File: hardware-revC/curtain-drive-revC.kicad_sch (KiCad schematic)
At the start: 45 parts, among them J1 12V IN, J3 MOTOR, J4 ENCODER I2C, J5 UART, SW1 USER, SW2 BOOT, SW3 RESET, U1 ESP32-WROOM-32, U2 L298, U3 LM2575T-ADJ, U4 LM7805

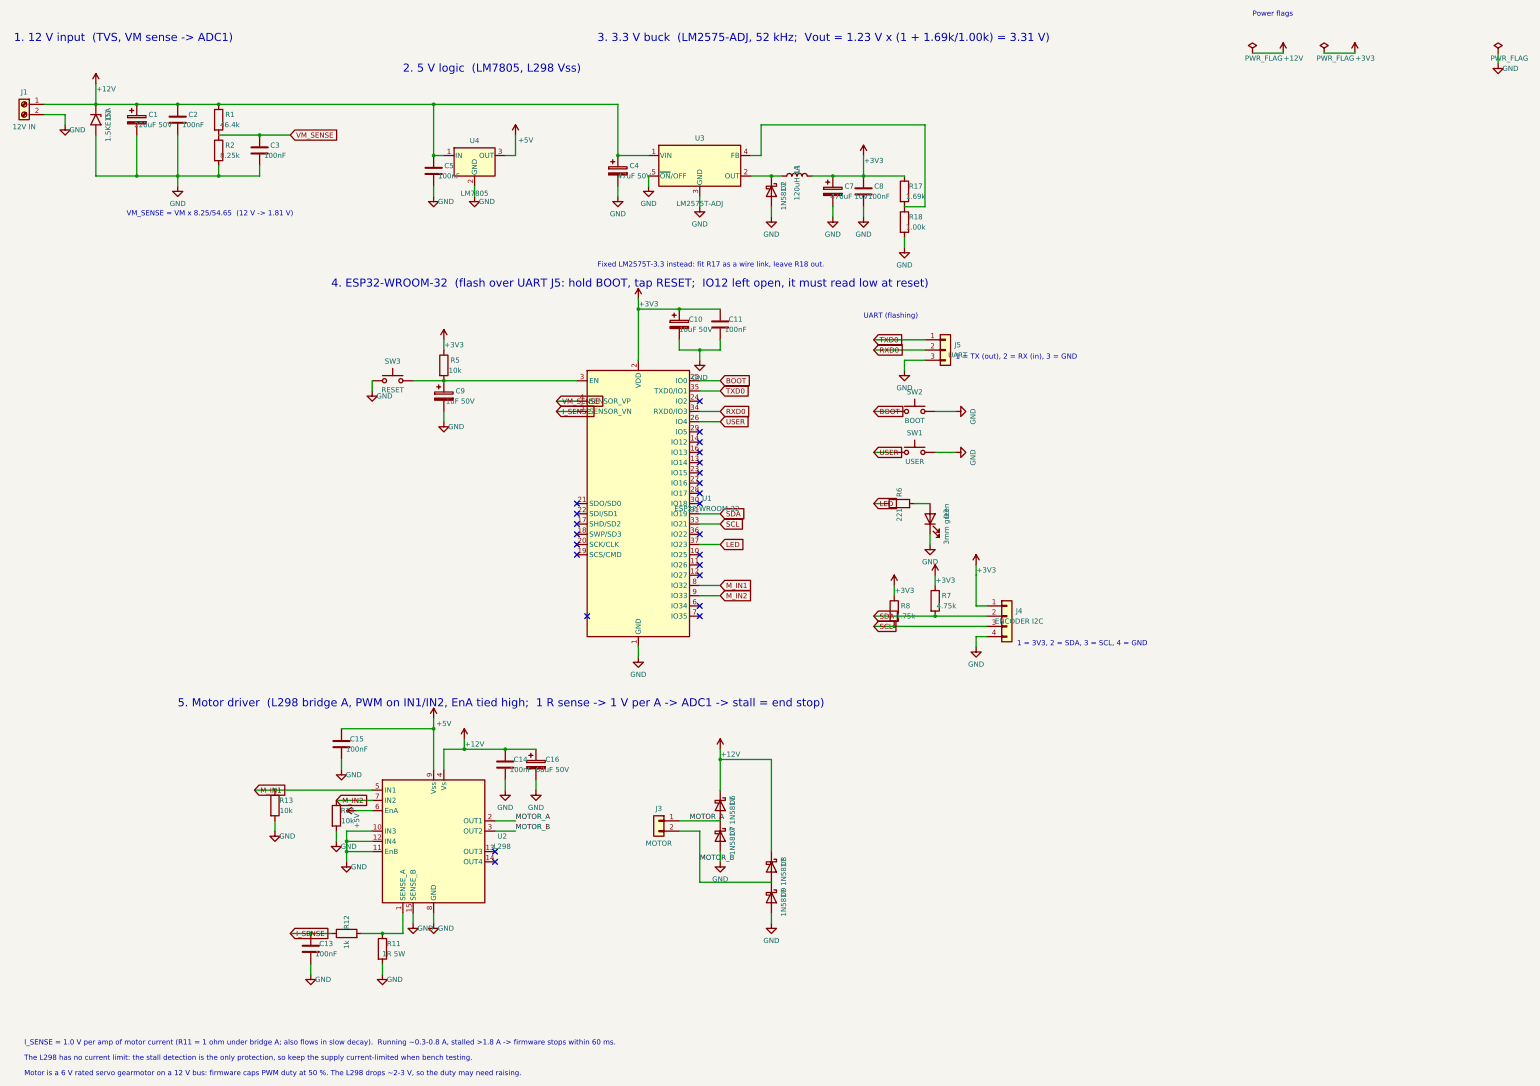
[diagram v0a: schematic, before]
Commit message: Rev C: proven LM317 supply for the WROOM-32, 470 uF at the module
Rework rev C to the ESP32 recipe that ran on real hardware
(esp32-solder-test). The LM2575 buck was untested with the shop's 120 uH
inductor; the 3.3 V rail now comes from an LM317T (243R/392R, 3.27 V) fed
from 12 V through a 1N5817, with a 1N4003 reverse-protection diode, 10 uF +
100 nF at its input and 10 uF at its output. It needs the shop's TO-220
heatsink at 12 V, and its tab faces a cleared area at the bottom edge.

The 470 uF bulk cap moves onto the module's 3V3 line, on a 0.8 mm track:
a 10 uF rail collapsed under the Wi-Fi TX peaks on the test board. IO0
gets its 10k pull-up (R15), and the firmware caps TX power at 8.5 dBm.

Re-routed with FreeRouting, 0 unconnected and DRC clean apart from silk
and courtyard margins. Laser and per-layer DXFs, drill file, schematic PDF
and BOM regenerated.

Co-Authored-By: Claude Opus 5.5 (1M context) <noreply@anthropic.com>
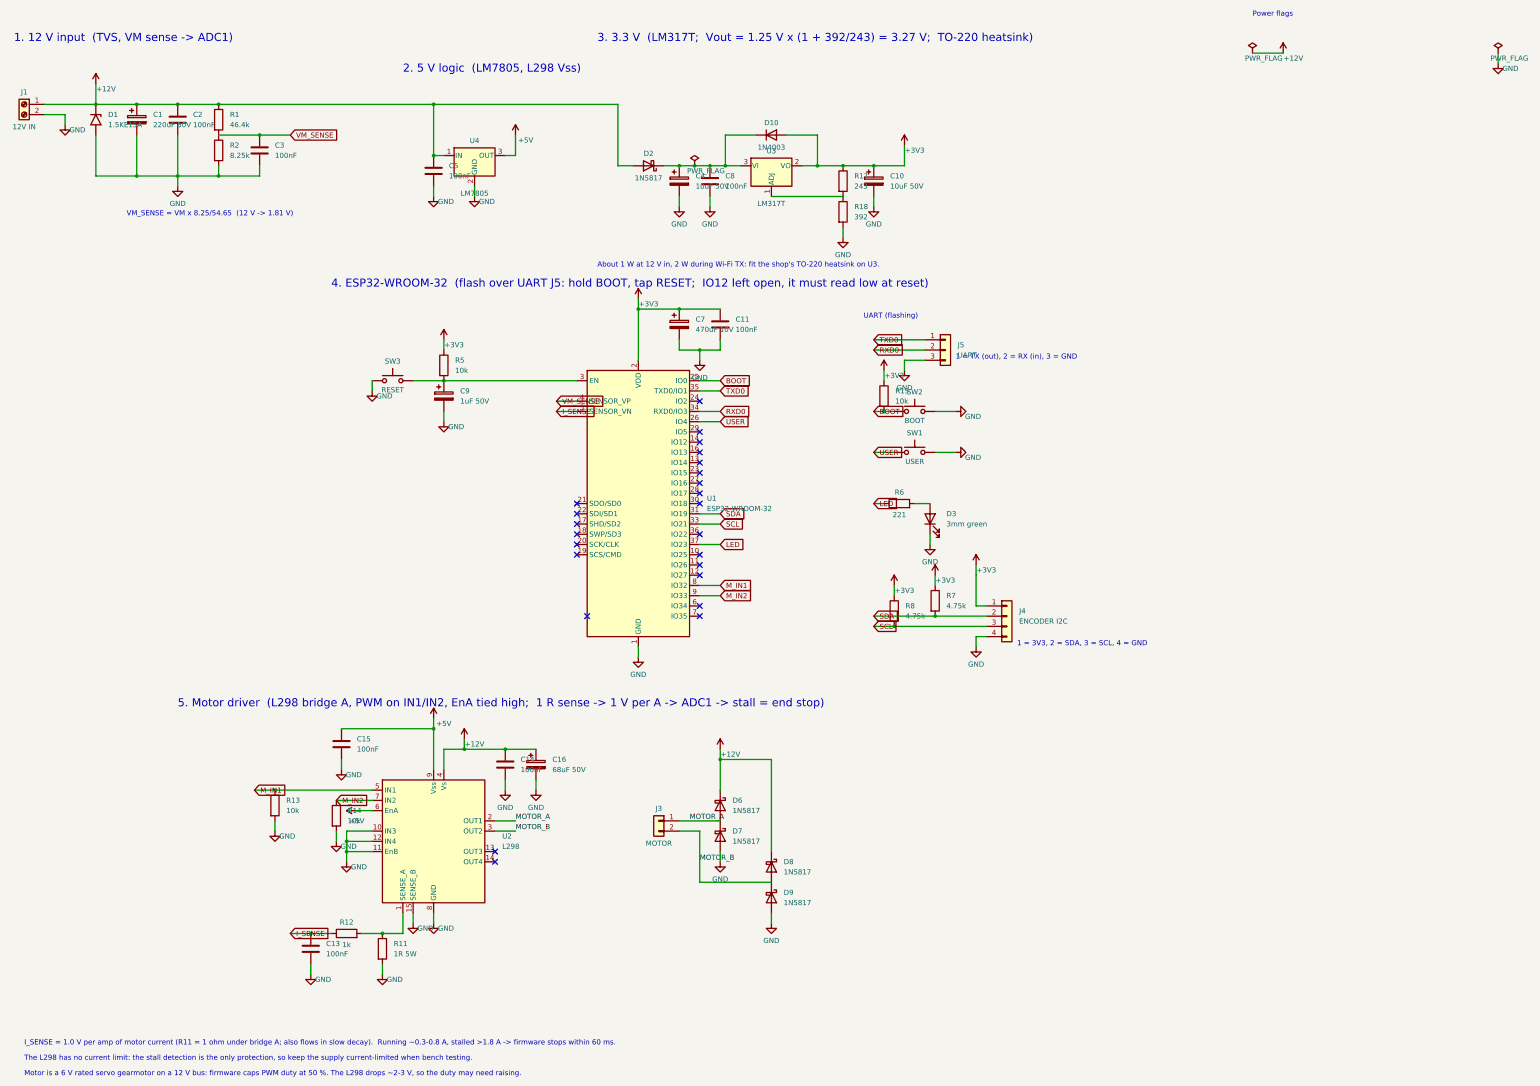
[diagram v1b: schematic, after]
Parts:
- removed L1: 120uH 1A, Inductor_THT:L_Radial_D10.0mm_P5.00mm_Fastron_07M, symbol Device:L
- removed U3: LM2575T-ADJ, CurtainDrive:TO-220-5_Vertical_LongPads, symbol Regulator_Switching:LM2575BT-ADJ
- added D10: 1N4003, Diode_THT:D_DO-41_SOD81_P10.16mm_Horizontal, symbol Device:D
- added R15: 10k, Resistor_THT:R_Axial_DIN0207_L6.3mm_D2.5mm_P7.62mm_Horizontal, symbol Device:R
- added U3: LM317T, Package_TO_SOT_THT:TO-220-3_Vertical, symbol Regulator_Linear:LM317_TO-220
- C4: value 47uF 50V -> 10uF 50V; footprint Capacitor_THT:CP_Radial_D6.3mm_P2.50mm -> Capacitor_THT:CP_Radial_D5.0mm_P2.00mm
- R17: value 1.69k -> 243
- R18: value 1.00k -> 392
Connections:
- net +12V: now also D2.2 (A); no longer C4.1
- net +3V3: now also D10.2 (A), R15.1, U3.2 (VO); no longer C8.1
- net BOOT: now also R15.2
- net GND: no longer D2.2 (A)
- net at D2.1 (K): now also C4.1, C8.1, D10.1 (K), U3.3 (VI)
- net at R17.2, R18.1: now also U3.1 (ADJ)
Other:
- note added: "3. 3.3 V (LM317T; Vout = 1.25 V x (1 + 392/243) = 3.27 V; TO-220 heatsink)"
- note added: "About 1 W at 12 V in, 2 W during Wi-Fi TX: fit the shop's TO-220 heatsink on U3."
- note removed: "3. 3.3 V buck (LM2575-ADJ, 52 kHz; Vout = 1.23 V x (1 + 1.69k/1.00k) = 3.31 V)"
- note removed: "Fixed LM2575T-3.3 instead: fit R17 as a wire link, leave R18 out."

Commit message: Rev C: pin holes and keep-out for U3's pin-mount heatsink
The shop's TO-220 heatsink (16 x 16 x 25.4 mm) stands on two 2.3 mm pins,
10.2 mm apart, with their centres 2.5 mm behind the face the LM317's tab
bolts to. U3 gets its own footprint with those two 2.6 mm unplated holes
(5.65 mm behind the leg row, centred on OUT) and a courtyard covering the
heatsink, so the laser cut file carries the holes and no part lands under it.

U3 moves up to y = 52 so the heatsink ends inside the board edge; R17, R18,
D10, C10, C4 and C8 re-placed around it. Re-routed: 0 unconnected, DRC
clean apart from silk and courtyard margins. DXFs, drill file, PDF and
build notes regenerated.

Co-Authored-By: Claude Opus 5.5 (1M context) <noreply@anthropic.com>
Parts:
- U3: footprint Package_TO_SOT_THT:TO-220-3_Vertical -> CurtainDrive:TO-220-3_Vertical_Heatsink16x16
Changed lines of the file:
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@@
 			)
 		)
-		(property "Footprint" "Package_TO_SOT_THT:TO-220-3_Vertical"
+		(property "Footprint" "CurtainDrive:TO-220-3_Vertical_Heatsink16x16"
 			(at 198.12 50.8 0)
 			(hide yes)
